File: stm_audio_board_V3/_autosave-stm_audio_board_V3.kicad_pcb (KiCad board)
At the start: 4 copper layers, 201 x 117 mm, 258 parts, among them J1 Power conn, J10 USB_A, J11 AudioJack_Loop1_Return, J12 AudioJack_Loop1_Send, J13 AudioJack_INPUT_Main, J14 AudioJack_OUTPUT_Main, J15 AudioJack_Loop2_Send, J16 STlink_DISP_MCU, J2 STlink_DSP, J3 Audio_sig, J4 Conn_01x01_taptempo, J5 Barrel_Jack_MountingPin, J6 Conn_01x03_pot_ext, J7 AudioJack_Loop3_Return, J8 AudioJack_Loop3_Send, J9 AudioJack_Loop2_Return, SW1 SW_SPST, SW2 SW_SPST, U1 IS42S16100H-7TL, U10 OP275, U12 OP275, U13 LM7809_TO220, U14 OP275, U15 STM32H723ZGTx, U16 LM7909_TO220, U2 OP275, U3 R-78B5.0-2.0, U4 OP275, U5 MIC2920A-3.3WS-TR, U7 STM32H723ZGTx, U8 OP275, U9 MIC2920A-3.3WS-TR, Y1 X1E0000210132, Y2 X1E0000210132

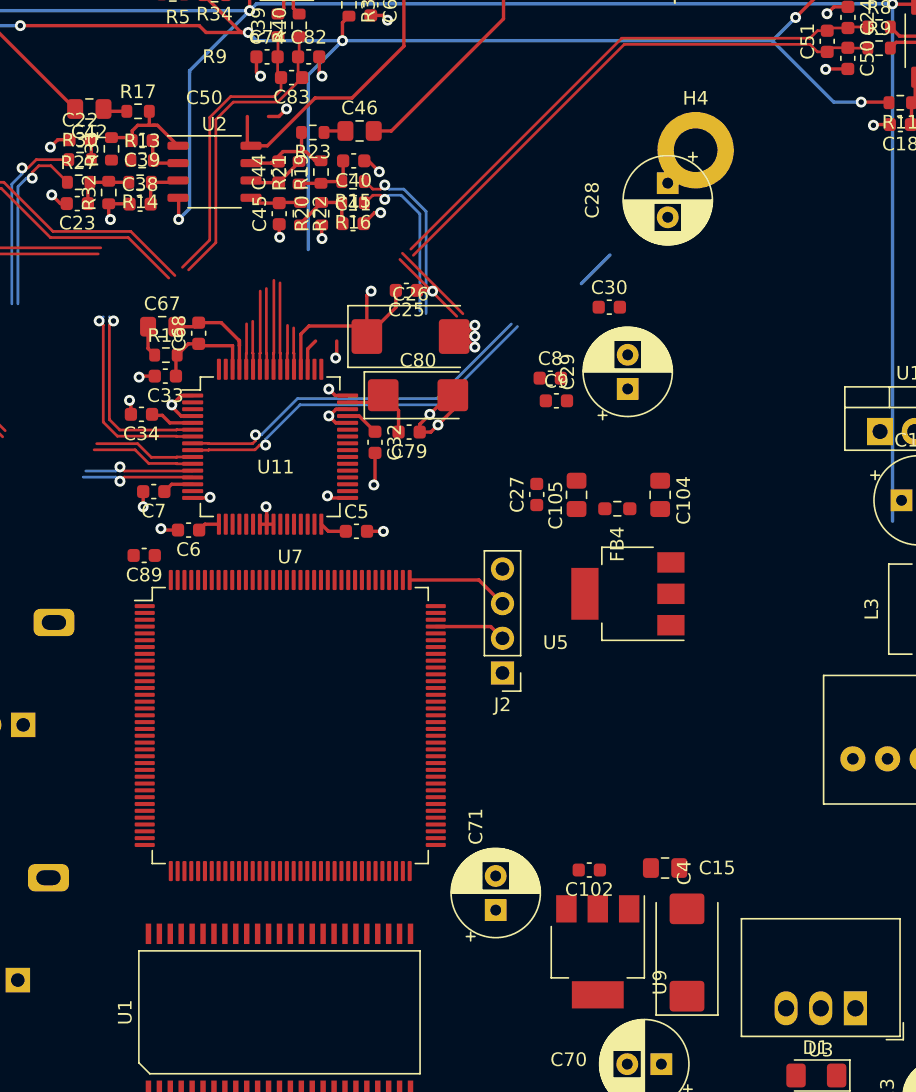
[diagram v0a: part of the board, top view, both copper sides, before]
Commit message: +-12 DCDC added
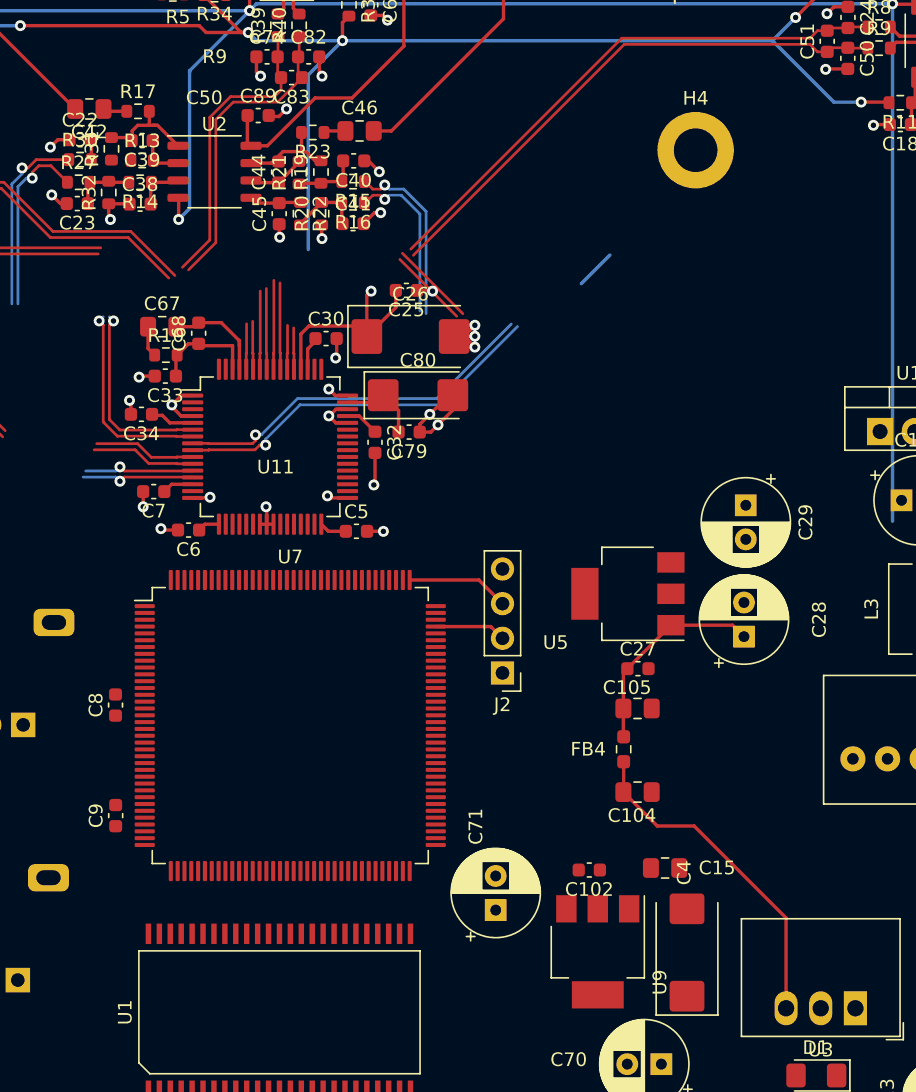
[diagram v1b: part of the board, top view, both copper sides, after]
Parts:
- moved C9 44.3 mm to (194.4, 122.0), turned to 90 degrees
- moved C8 39.9 mm to (194.4, 113.9), turned to 90 degrees
- moved C28 33.7 mm to (240.4, 108.9), turned to 90 degrees
- moved C89 33.3 mm to (204.8, 70.7), turned to 0 degrees
- moved C104 21.8 mm to (232.6, 120.3), turned to 0 degrees
- moved C30 20.9 mm to (209.8, 87.0)
- moved FB4 17.6 mm to (231.6, 117.1), turned to 90 degrees
- moved C105 16.3 mm to (232.6, 114.1), turned to 0 degrees
- moved C27 14.8 mm to (232.6, 111.2), turned to 0 degrees
- moved C29 12.1 mm to (240.6, 99.2), turned to -90 degrees
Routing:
- net 5V: track 0.00 -> 24.6 mm
- net Net-(U5-VI): track 0.00 -> 15.3 mm

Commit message: isolated power section done
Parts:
- removed D1: 1N4148, Diode_SMD:D_1206_3216Metric_Pad1.42x1.75mm_HandSolder
- removed FB4: TDK MMZ1608R601ATD25 DB, Resistor_SMD:R_0603_1608Metric_Pad0.98x0.95mm_HandSolder
- removed U3: R-78B5.0-2.0, Converter_DCDC:Converter_DCDC_RECOM_R-78B-2.0_THT
- added C103: 10uF, Capacitor_SMD:C_1206_3216Metric, F.Cu at (283.5, 119.1)
- added C136: 10uF, Capacitor_SMD:C_1206_3216Metric, F.Cu at (270.0, 142.7)
- added C137: 10uF, Capacitor_SMD:C_1206_3216Metric, F.Cu at (286.3, 119.1)
- added C138: 10uF, Capacitor_SMD:C_1206_3216Metric, F.Cu at (272.2, 116.8)
- added C139: 10uF, Capacitor_SMD:C_1206_3216Metric, F.Cu at (324.3, 102.2)
- added C140: 100uF, Capacitor_THT:CP_Radial_D6.3mm_P2.50mm, F.Cu at (314.6, 85.3)
- added C141: 10uF, Capacitor_SMD:C_1206_3216Metric, F.Cu at (324.3, 105.5)
- added C142: 10uF, Capacitor_SMD:C_1206_3216Metric, F.Cu at (324.3, 108.9)
- added C143: 10uF, Capacitor_SMD:C_1206_3216Metric, F.Cu at (324.3, 112.2)
- added C144: 10uF, Capacitor_SMD:C_1206_3216Metric, F.Cu at (329.9, 95.5)
- added C145: 10uF, Capacitor_SMD:C_1206_3216Metric, F.Cu at (329.9, 98.8)
- added C146: 10uF, Capacitor_SMD:C_1206_3216Metric, F.Cu at (329.9, 102.2)
- added C147: 10uF, Capacitor_SMD:C_1206_3216Metric, F.Cu at (329.9, 105.5)
- added C148: 10uF, Capacitor_SMD:C_1206_3216Metric, F.Cu at (322.6, 83.1)
- added C149: 10uF, Capacitor_SMD:C_1206_3216Metric, F.Cu at (322.6, 86.4)
- added C150: 100uF, Capacitor_THT:CP_Radial_D6.3mm_P2.50mm, F.Cu at (314.6, 93.2)
- added C151: 100uF, Capacitor_THT:CP_Radial_D6.3mm_P2.50mm, F.Cu at (314.6, 101.0)
- added C152: 10uF, Capacitor_SMD:C_1206_3216Metric, F.Cu at (322.6, 89.8)
- added C153: 10uF, Capacitor_SMD:C_1206_3216Metric, F.Cu at (322.6, 93.1)
- added C154: 10uF, Capacitor_SMD:C_1206_3216Metric, F.Cu at (322.6, 96.5)
- added C155: 10uF, Capacitor_SMD:C_1206_3216Metric, F.Cu at (322.6, 99.8)
- added C48: 100uF, Capacitor_THT:CP_Radial_D6.3mm_P2.50mm, F.Cu at (284.5, 133.6)
- added C69: 100uF, Capacitor_THT:CP_Radial_D6.3mm_P2.50mm, F.Cu at (270.6, 134.9)
- added C75: 100uF, Capacitor_THT:CP_Radial_D6.3mm_P2.50mm, F.Cu at (284.3, 127.2)
- added C76: 100uF, Capacitor_THT:CP_Radial_D6.3mm_P2.50mm, F.Cu at (269.7, 129.4)
- added C77: 100uF, Capacitor_THT:CP_Radial_D6.3mm_P2.50mm, F.Cu at (261.8, 129.4)
- added L4: 10uH, Inductor_SMD:L_6.3x6.3_H3, F.Cu at (277.8, 141.6)
- added L5: 10uH, Inductor_SMD:L_6.3x6.3_H3, F.Cu at (229.0, 107.3)
- added L6: 10uH, Inductor_SMD:L_6.3x6.3_H3, F.Cu at (329.7, 85.3)
- added PS1: URB2405S-6WR3, Converter_DCDC:Converter_DCDC_XP_POWER-ITxxxxxS_THT, F.Cu at (265.4, 139.1)
- C104, C105: value 2u2F -> 10uF; footprint Capacitor_SMD:C_0805_2012Metric_Pad1.18x1.45mm_HandSolder -> Capacitor_SMD:C_1206_3216Metric
- C13: value 22uF 50V poly -> 100uF; footprint Capacitor_THT:CP_Radial_D5.0mm_P2.00mm -> Capacitor_THT:CP_Radial_D6.3mm_P2.50mm
- C132: value 100uF -> 10uF; footprint Capacitor_THT:CP_Radial_D6.3mm_P2.50mm -> Capacitor_SMD:C_1206_3216Metric
- C133: value 47uF -> 10uF; footprint Capacitor_THT:CP_Radial_D6.3mm_P2.50mm -> Capacitor_SMD:C_1206_3216Metric
- C15: value 2u2F -> 100uF; footprint Capacitor_SMD:C_0805_2012Metric_Pad1.18x1.45mm_HandSolder -> Capacitor_THT:CP_Radial_D6.3mm_P2.50mm
- C27: value 100n -> 100uF; footprint Capacitor_SMD:C_0603_1608Metric -> Capacitor_THT:CP_Radial_D6.3mm_P2.50mm
- C4: value 22uF tantal -> 100uF; footprint Capacitor_Tantalum_SMD:CP_EIA-7343-31_Kemet-D_Pad2.25x2.55mm_HandSolder -> Capacitor_THT:CP_Radial_D6.3mm_P2.50mm
- moved C132 64.0 mm to (272.6, 142.7), turned to -90 degrees
- moved C105 58.0 mm to (283.1, 142.7), turned to -90 degrees
- moved C104 57.6 mm to (285.7, 142.7), turned to -90 degrees
- moved C27 33.6 mm to (254.4, 85.6), turned to 180 degrees
- moved C28 31.7 mm to (261.9, 85.6), turned to 0 degrees
- moved J5 30.4 mm to (291.1, 129.9)
- moved C13 28.2 mm to (279.8, 130.6), turned to 180 degrees
- moved C15 27.9 mm to (235.4, 97.9)
- moved C70 26.6 mm to (229.7, 114.0), turned to -90 degrees
- moved C4 21.9 mm to (236.2, 110.1), turned to -90 degrees
- moved C102 20.0 mm to (233.8, 106.6), turned to 0 degrees
- moved L1 15.9 mm to (277.7, 117.9), turned to 180 degrees
- moved C119 14.4 mm to (260.8, 56.4), turned to 0 degrees
- moved C133 14.0 mm to (269.4, 116.8)
- moved R7 13.8 mm to (261.7, 59.3), turned to -90 degrees
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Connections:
- C104 pad 1: 5V -> PWR_INPUT_12V-18V
- C104 pad 2: GND -> Earth
- C105 pad 1: Net-(U5-VI) -> PWR_INPUT_12V-18V
- C105 pad 2: GND -> Earth
- C13 pad 2: GND -> Earth
- C132 pad 1: PWR_INPUT_12V-18V -> Net-(PS1-+Vin)
- C132 pad 2: GND -> Earth
- C133 pad 2: GND -> Earth
- C15 pad 1: 5V -> Net-(U5-VI)
- C27 pad 1: Net-(U5-VI) -> GND
- C27 pad 2: GND -> -9V
- C28 pad 1: Net-(U5-VI) -> +9V
- J5 pad 2: GND -> Earth
- PS2 pad 1: GND -> Earth
- U13 pad 3: unconnected-(U13-VO-Pad3) -> +9V
- U16 pad 3: unconnected-(U16-VO-Pad3) -> -9V
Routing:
- net +9V: track 245.3 -> 196.8 mm, vias 6 -> 5
- net ADC1N: track 43.5 -> 6.32 mm
- net ADC1P: track 43.1 -> 6.15 mm
- net GND: track 90.7 -> 117.4 mm
- net 5V: track 24.6 -> 0.00 mm
- net PWR_INPUT_12V-18V: track 0.00 -> 19.1 mm
- net AD1939_CM: track 216.2 -> 197.1 mm, vias 12 -> 10
- net Net-(PS2-+Vin): track 0.00 -> 15.9 mm
- net Net-(U5-VI): track 15.3 -> 0.00 mm
- net Net-(PS1-+Vin): track 0.00 -> 8.89 mm
- net Audio_Main_Input: track 12.2 -> 6.80 mm
- net Earth: vias 0 -> 25
- added copper zone on F.Cu, net Earth
- added copper zone on In1.Cu, net Earth
- added copper zone on In2.Cu, net Earth
- added copper zone on F.Cu, net Net-(PS1-+Vin)
- added copper zone on F.Cu, net PWR_INPUT_12V-18V
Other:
- board size 201 x 117 mm -> 230.9 x 117 mm

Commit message: minor power section fixes
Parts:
- moved C148 103.7 mm to (237.3, 142.0), turned to -90 degrees
- moved L6 103.1 mm to (239.9, 136.0), turned to 180 degrees
- moved C149 97.4 mm to (242.7, 142.1), turned to -90 degrees
- moved C140 96.9 mm to (232.0, 136.0), turned to 180 degrees
- moved C151 92.7 mm to (232.1, 143.2), turned to 180 degrees
- moved C150 90.0 mm to (232.0, 128.9), turned to 180 degrees
- moved C145 81.8 mm to (249.2, 86.1), turned to 180 degrees
- moved C144 81.0 mm to (249.2, 88.6), turned to 180 degrees
- moved C141 80.5 mm to (243.8, 105.9), turned to -90 degrees
- moved C139 78.0 mm to (246.4, 105.9), turned to -90 degrees
- moved C154 74.4 mm to (248.9, 105.9), turned to -90 degrees
- moved C147 70.4 mm to (261.5, 88.7)
- moved C146 70.2 mm to (261.5, 86.3)
- moved C155 69.1 mm to (254.4, 88.6)
- moved C143 59.3 mm to (265.3, 106.0), turned to -90 degrees
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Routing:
- net 5V: track 0.00 -> 32.3 mm
- net Net-(U16-VI): track 0.00 -> 26.3 mm
- net Net-(U13-VI): track 0.00 -> 25.9 mm
- net /Power/-12V: track 0.00 -> 23.6 mm
- net /Power/+12V: track 0.00 -> 22.8 mm
- net Net-(PS1-+Vout): track 0.00 -> 16.3 mm
- net -9V: track 225.8 -> 237.0 mm
- net GND: track 117.4 -> 128.4 mm, vias 56 -> 77
- net +9V: track 196.8 -> 206.1 mm
- net Net-(PS1-+Vin): track 8.89 -> 9.46 mm
- added copper zone on F.Cu, net GND
